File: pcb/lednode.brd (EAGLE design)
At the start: 99.8 x 49.8 mm, 50 parts, among them Q1 AO3402, Q2 AO3402, Q3 AO3402, Q4 AO3402, Q5 AO3402, Q6 AO3402

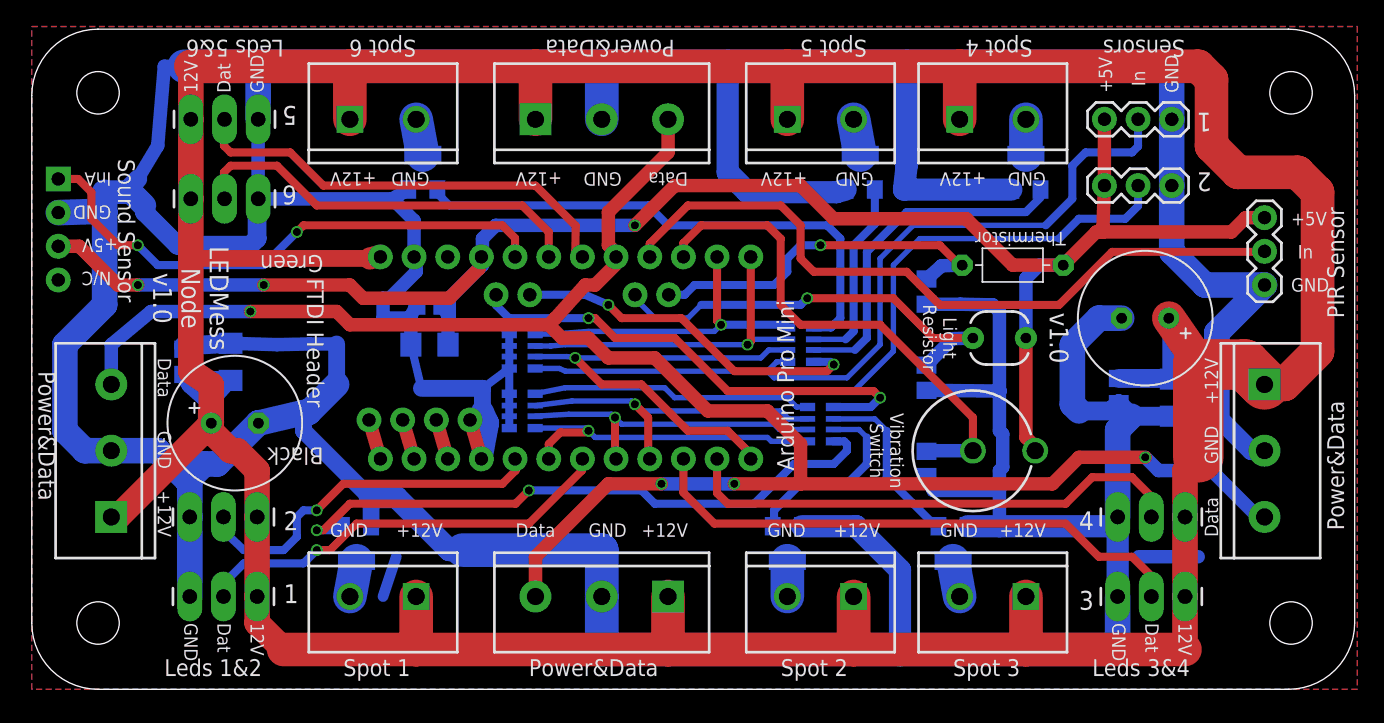
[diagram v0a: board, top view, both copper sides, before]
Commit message: Removed old versions of the lednode and removed version numbers from the filenames.
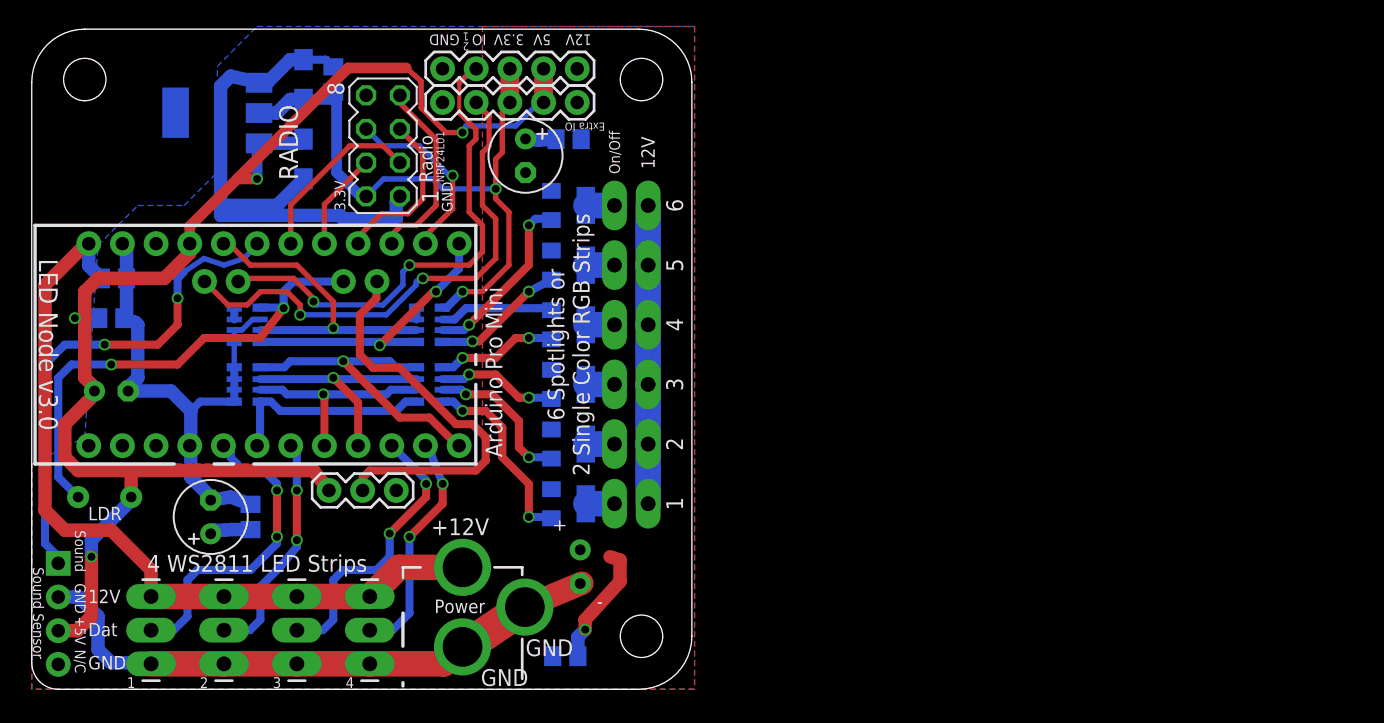
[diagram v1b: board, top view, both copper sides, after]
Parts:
- removed GND, RESET, RXI, TXO: M01SMDNS, SparkFun-Connectors:1X01NS
- removed LEDS5, LEDS6: (no value), SparkFun-Connectors:1X03_LONGPADS
- removed NEIGHBOR1, NEIGHBOR2, NEIGHBOR3, NEIGHBOR4: (no value), SparkFun-Connectors:SCREWTERMINAL-5MM-3
- removed R1, R2, R3: 10k, rcl:R0805
- removed SENSOR1, SENSOR2: (no value), SparkFun-Connectors:1X03
- removed SHAKE: SW-18010P, sensor-comus-group:CM4400
- removed THERM: 10k, discrete-fixed-thermistor-silk:R-7,5
- added 3.3V_REG: AMS1117-3.3, burr-brown:SOT223
- added C10, C13: 100 nF, rcl:C0805
- added C12: 22uF Tant, rcl:SMC_A
- added C9: 100 uF, rcl:E2,5-6
- added IO1, IO2: (no value), SparkFun-Connectors:1X05
- added J1: POWER_JACKPTH, SparkFun-Connectors:POWER_JACK_PTH
- added RADIO: NRF24L01, con-lstb:MA04-2
- C1: device rcl:E3,5-10 -> rcl:E2,5-6
- C2: value 100 uF -> 100 nF; device rcl:E3,5-10 -> rcl:C0805
- C3: value 10 uF -> 100 nF; device rcl:C1206 -> rcl:C0805
- C4: value 10 uF -> 100 uF; device rcl:C1206 -> rcl:E2,5-6
- C7: value 10 uF -> 22uF Tant; device rcl:C1206 -> rcl:SMC_A
- C8: value 100 nF -> 100 uF; device rcl:C0805 -> rcl:E2,5-6
- SPOT1, SPOT2, SPOT3, SPOT4, SPOT5, SPOT6: value M025MM -> M02PTH3; device SparkFun-Connectors:SCREWTERMINAL-5MM-2 -> SparkFun-Connectors:1X02_LONGPADS
- moved C4 80.0 mm to (6.00, 22.5), turned to 180 degrees
- moved C1 72.1 mm to (13.5, 13.0), turned to 90 degrees
- moved PHOTOCELL 68.6 mm to (5.50, 14.5), flipped to the bottom, turned to 180 degrees
- moved PIR 67.3 mm to (27.5, 15.0), turned to 180 degrees
- moved LEDS3 67.0 mm to (20.0, 7.00), turned to 270 degrees
- moved LOGO3 62.2 mm to (0.75, 38.8), turned to 90 degrees
- moved LEDS4 61.8 mm to (25.5, 7.00), turned to 270 degrees
- moved C6 45.6 mm to (40.5, 41.5), turned to 180 degrees
- moved Q4 36.4 mm to (40.5, 27.5), turned to 90 degrees
- moved SPOT3 32.7 mm to (46.5, 23.0)
- moved Q3 31.4 mm to (40.5, 23.0), turned to 90 degrees
- moved RN1 29.7 mm to (30.0, 23.0)
- moved SOUND_SENSOR 29.0 mm to (2.00, 9.50)
- moved SPOT4 28.2 mm to (46.5, 27.5), turned to 180 degrees
- moved RN3 28.0 mm to (30.0, 27.5)
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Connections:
- removed net DATA_BUS: NEIGHBOR1.3, NEIGHBOR2.3, NEIGHBOR3.3, NEIGHBOR4.3, U$1.17
- removed net EXTRA_SENSOR1: RN3.8, U$1.A4
- removed net EXTRA_SENSOR2: RN1.5, U$1.A5
- removed net LEDSTRIP5: LEDS5.2, U$1.18
- removed net LEDSTRIP6: LEDS6.2, U$1.19
- removed net N$15: RXI.1, U$1.2
- removed net N$16: RESET.1, U$1.3
- removed net SENSOR1: RN3.1, RN4.8, SENSOR1.2
- removed net SHAKE: R1.2, SHAKE.1, U$1.15
- removed net TEMPERATURE: R2.2, THERM.2, U$1.A6
- new net +3V3: 3.3V_REG.2, C12.+, C13.1, IO1.3, IO2.3, RADIO.2, RN3.5
- new net EXTRA_IO1: IO1.2, U$1.A4
- new net EXTRA_IO2: IO2.2, U$1.A5
- new net RADIO_CE: RADIO.3, U$1.18
- new net RADIO_CSN: RADIO.4, U$1.17
- new net RADIO_IRQ: RADIO.8
- new net RADIO_MISO: RADIO.7, U$1.15
- new net RADIO_MOSI: RADIO.6, U$1.14
- new net RADIO_SCK: RADIO.5, U$1.16
- net +12V: now also C10.1, C8.+, C9.+, IO1.5, IO2.5, J1.PWR; no longer C2.+, C4.1, LEDS5.1, LEDS6.1, NEIGHBOR1.1, NEIGHBOR2.1, NEIGHBOR3.1, NEIGHBOR4.1
- net +5V: now also 3.3V_REG.3, C2.1, C4.+, C7.+, IO1.4, IO2.4; no longer C7.1, C8.1, SENSOR1.3, SENSOR2.3, SHAKE.2, THERM.1
- net GND: now also 3.3V_REG.1, C10.2, C12.-, C13.2, C2.2, C4.-, C7.-, C8.-, C9.-, IO1.1, IO2.1, J1.GND, J1.GNDBREAK, RADIO.1, RN3.6, RN4.6; no longer C2.-, C4.2, C7.2, C8.2, GND.1, LEDS5.3, LEDS6.3, NEIGHBOR1.2, NEIGHBOR2.2, NEIGHBOR3.2, NEIGHBOR4.2, R1.1, R2.1, R3.1, RN4.3, RN4.4, SENSOR1.1, SENSOR2.1
- net LEDSTRIP1: now also U$1.5; no longer U$1.7
- net LEDSTRIP2: now also U$1.7; no longer U$1.5
- net LIGHTLEVEL: now also RN4.5; no longer R3.2
- net N$10: now also RN3.8; no longer RN3.6
- net N$12: now also RN4.3, RN4.4; no longer Q6.1, RN3.5
- net N$13: now also Q6.1, RN3.7; no longer RN1.4, RN2.5, SENSOR2.2
- net N$14: now also RN3.3, RN3.4; no longer TXO.1, U$1.1
- net N$8: now also RN1.5; no longer RN3.7
- net PROXIMITY: now also U$1.A6; no longer U$1.16
- net SOUND_ANALOG: now also U$1.19; no longer U$1.20
- net SPOTLIGHT4: now also RN1.4, RN2.5; no longer RN3.2, RN4.7
- net SPOTLIGHT5: now also RN3.1, RN4.8; no longer RN3.3, RN4.6
- net SPOTLIGHT6: now also RN3.2, RN4.7, U$1.20; no longer RN3.4, RN4.5, U$1.14
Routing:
- net GND: track 497.2 -> 134.6 mm
- net +12V: track 336.0 -> 98.1 mm, vias 0 -> 1
- net DATA_BUS: track 146.1 -> 0.00 mm, vias 4 -> 0
- net SENSOR1: track 62.1 -> 0.00 mm
- net +3V3: track 0.00 -> 47.9 mm, vias 0 -> 2
- net N$13: track 59.0 -> 13.5 mm, vias 0 -> 2
- net N$12: track 40.5 -> 0.90 mm
- net EXTRA_IO2: track 0.00 -> 39.0 mm, vias 0 -> 2
- net SHAKE: track 38.4 -> 0.00 mm
- net EXTRA_IO1: track 0.00 -> 37.3 mm, vias 0 -> 2
- net EXTRA_SENSOR2: track 36.5 -> 0.00 mm, vias 2 -> 0
- net LEDSTRIP5: track 33.9 -> 0.00 mm
- net N$6: track 47.4 -> 14.7 mm
- net LEDSTRIP6: track 30.7 -> 0.00 mm
- net TEMPERATURE: track 27.9 -> 0.00 mm, vias 1 -> 0
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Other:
- board size 99.8 x 49.8 mm -> 49.8 x 49.8 mm
- board text added: "+"
- board text added: "-"
- board text added: "3.3V"
- board text added: "4 WS2811 LED Strips"
- board text added: "5V"
- board text added: "6 Spotlights or 2 Single Color RGB Strips"
- board text added: "Extra IO"
- board text added: "IO"
- board text added: "LDR"
- board text added: "LED Node v3.0"
- board text added: "NRF24L01"
- board text added: "On/Off"
- board text added: "Power"
- board text added: "Radio"
- board text added: "Sound"
- board text added: "github.com/zzorn/ledmesh"
- board text removed: "Black"
- board text removed: "Data"
- board text removed: "FTDI Header"
- board text removed: "Green"
- board text removed: "In"
- board text removed: "InA"
- board text removed: "LDR Volt Div"
- board text removed: "LEDMess Node v1.0"
- board text removed: "Leds 1&2"
- board text removed: "Leds 3&4"
- board text removed: "Leds 5&6"
- board text removed: "Light Resistor"
- board text removed: "Power&Data"
- board text removed: "RST"
- board text removed: "RXI"
- board text removed: "Sensors"
- board text removed: "Spot 1"
- board text removed: "Spot 2"
- board text removed: "Spot 3"
- board text removed: "Spot 4"
- board text removed: "Spot 5"
- board text removed: "Spot 6"
- board text removed: "TXO"
- board text removed: "Therm Volt Div"
- board text removed: "Thermistor"
- board text removed: "Vibration Pulldown"
- board text removed: "Vibration Switch"
- board text removed: "github.com/zzorn/ledmess"
- board text removed: "v1.0"
